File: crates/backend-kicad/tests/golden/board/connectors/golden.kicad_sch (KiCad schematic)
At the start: 4 parts, among them J1 J, J2 J, J3 J, J4 J

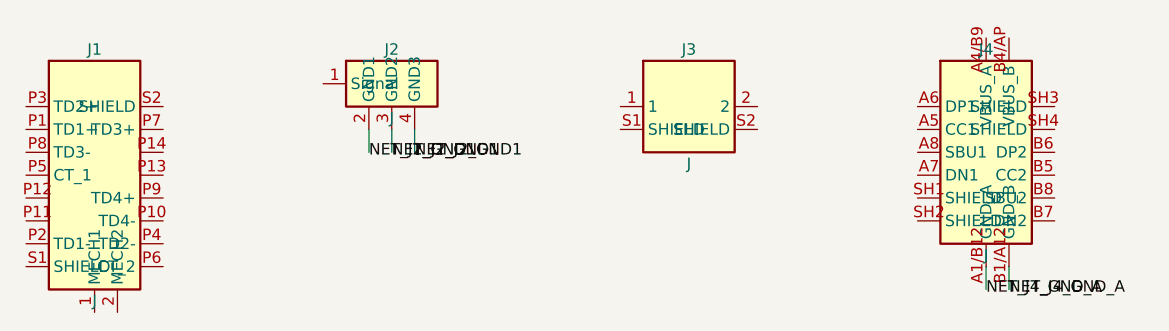
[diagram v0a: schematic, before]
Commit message: Improve recognition of bypass caps
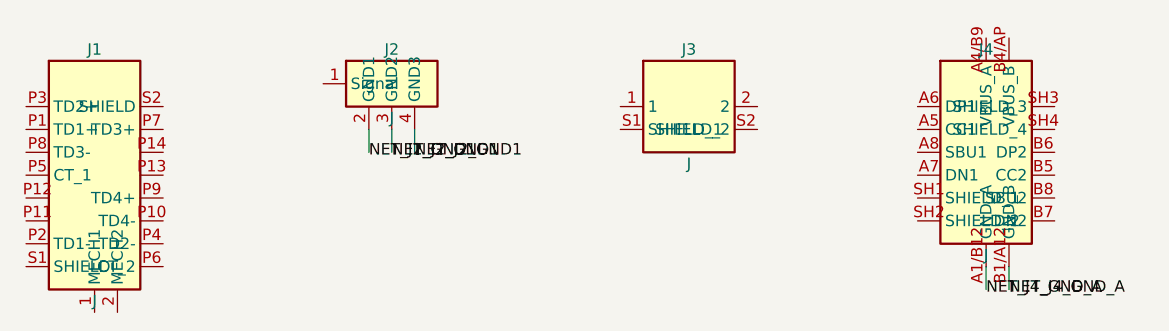
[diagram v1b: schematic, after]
